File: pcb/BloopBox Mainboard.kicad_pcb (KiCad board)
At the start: 4 copper layers, 65 x 44 mm, 61 parts, among them J1 ExtLED, J2 SPKR, J3 Raspberry_Pi, J4 I2C, J5 NFC-Module, J6 GPIO, J7 TailBoard, J8 PROG, Q1 2N7002, Q2 2N7002, Q3 2N7002, Q4 2N7002, Q5 2N7002, Q6 2N7002, U1 MAX98357, U2 CAT24C32

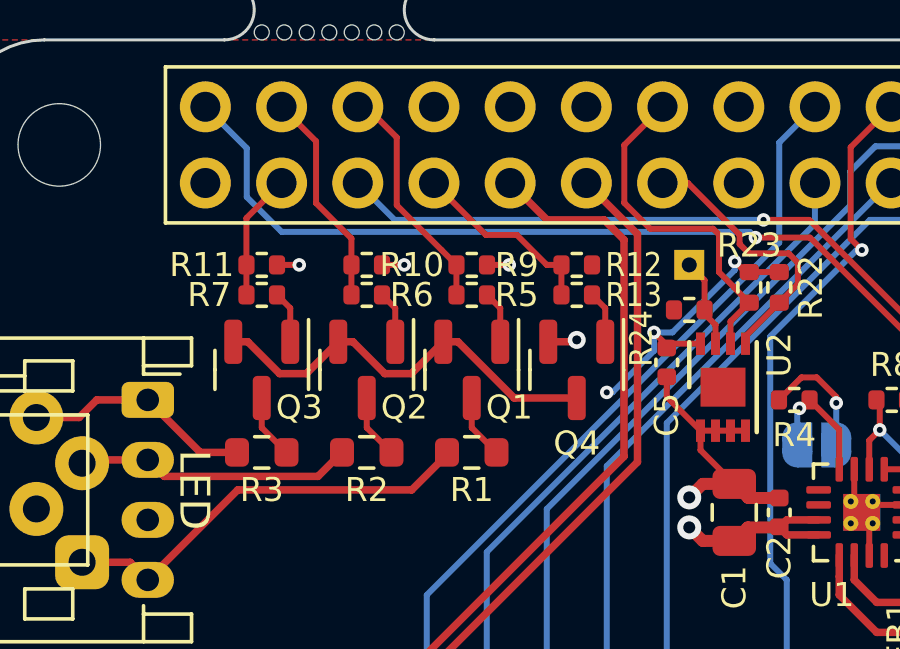
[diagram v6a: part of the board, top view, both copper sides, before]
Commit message: fix: update nets
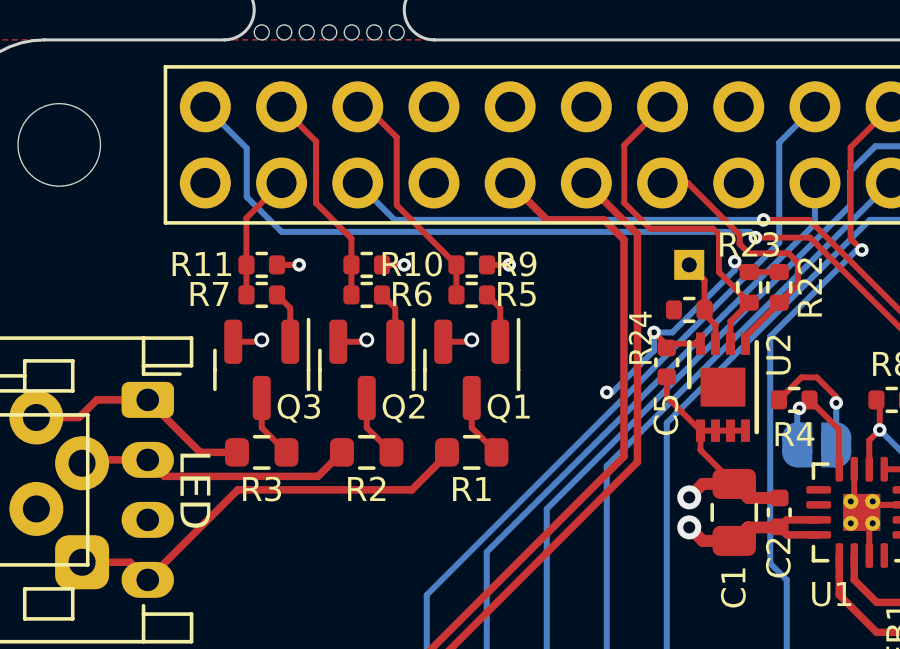
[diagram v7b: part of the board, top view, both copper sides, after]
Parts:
- removed Q4: 2N7002, Package_TO_SOT_SMD:SOT-23
- removed R12: 10k, Resistor_SMD:R_0402_1005Metric
- removed R13: 100R, Resistor_SMD:R_0402_1005Metric
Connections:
- J3 pad 33: /LED_PWM -> unconnected-(J3-Pad33)
- Q1 pad 2: /Pd -> GND
- Q2 pad 2: /Pd -> GND
- Q3 pad 2: /Pd -> GND
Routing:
- net /Pd: track 14.0 -> 0.00 mm
- net /LED_PWM: track 6.38 -> 0.00 mm
- net GND: track 17.0 -> 18.9 mm, vias 7 -> 9
- net /Pg: track 1.74 -> 0.00 mm

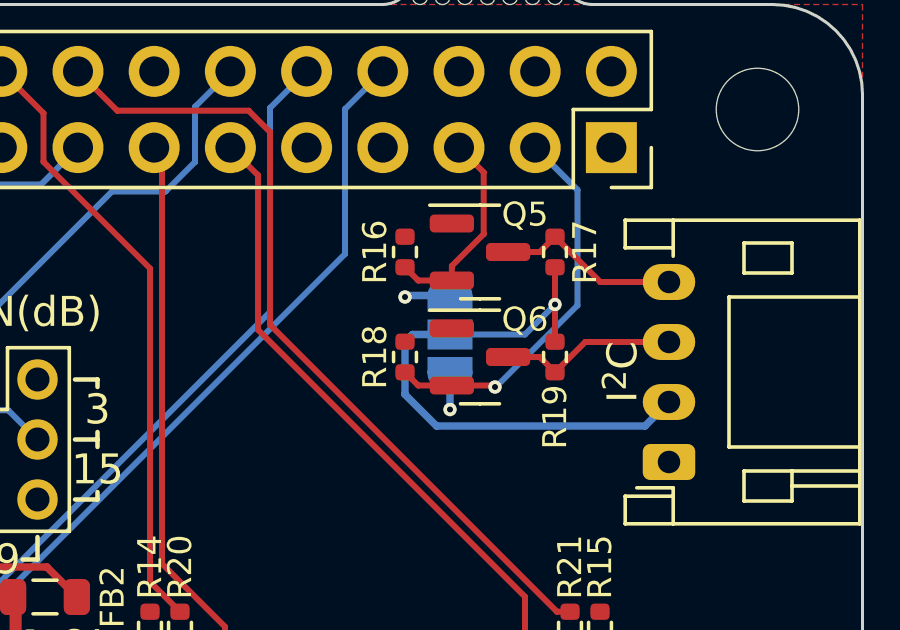
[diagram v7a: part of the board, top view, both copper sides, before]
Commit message: fix: add default connection for I2C voltage jumper
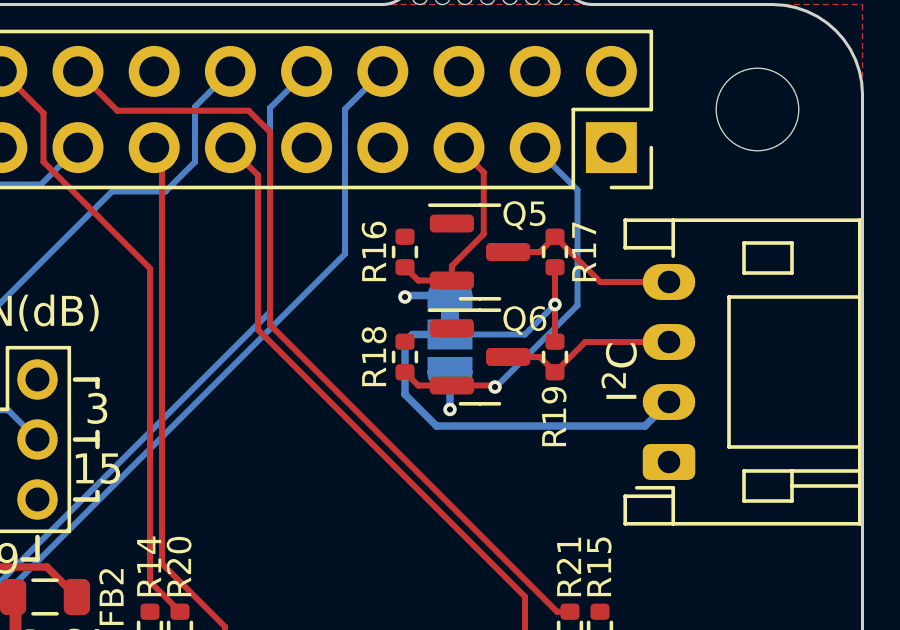
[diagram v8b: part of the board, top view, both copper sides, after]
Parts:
- JP3: value I2C Voltage-Select -> SolderJumper_3_Bridged12; footprint Jumper:SolderJumper-3_P1.3mm_Open_RoundedPad1.0x1.5mm -> Jumper:SolderJumper-3_P1.3mm_Bridged12_RoundedPad1.0x1.5mm
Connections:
- JP3 pad 1: +3V3 -> +5V
- JP3 pad 3: +5V -> +3V3
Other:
- board text added: "5V 3V3"
- board text removed: "3V3 5V"
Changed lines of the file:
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@@
     )
   )
-  (footprint "Jumper:SolderJumper-3_P1.3mm_Open_RoundedPad1.0x1.5mm" (layer "B.Cu")
+  (footprint "Jumper:SolderJumper-3_P1.3mm_Bridged12_RoundedPad1.0x1.5mm" (layer "B.Cu")
     (at 168.75 57.5 -90)
-    (descr "SMD Solder 3-pad Jumper, 1x1.5mm rounded Pads, 0.3mm gap, open")
-    (tags "solder jumper open")
+    (descr "SMD Solder 3-pad Jumper, 1x1.5mm rounded Pads, 0.3mm gap, pads 1-2 bridged with 1 copper strip")
+    (tags "net tie solder jumper bridged")
     (property "Sheetfile" "BloopBox Mainboard.kicad_sch")
     (property "Sheetname" "")
     (attr exclude_from_pos_files)
     (fp_text reference "JP3" (at 0 1.8 90) (layer "B.SilkS") hide
-      (effects (font (size 0.8 0.8) (thickness 0.15)) (justify mirror))
-    )
-    (fp_text value "I2C Voltage-Select" (at 0 -1.9 90) (layer "B.Fab")
       (effects (font (size 1 1) (thickness 0.15)) (justify mirror))
     )
+    (fp_text value "SolderJumper_3_Bridged12" (at 0 -1.9 90) (layer "B.Fab")
+      (effects (font (size 1 1) (thickness 0.15)) (justify mirror))
+    )
+    (fp_poly (pts
+        (xy -0.9 0.3)
+        (xy -0.4 0.3)
+        (xy -0.4 -0.3)
+        (xy -0.9 -0.3)
+      ) (layer "B.Cu") (width 0) (fill solid))
+    (fp_line (start 2.05 0.3) (end 2.05 -0.3) (layer "B.SilkS") (width 0.12))
+    (fp_line (start -1.2 -1.2) (end -1.5 -1.5) (layer "B.SilkS") (width 0.12))
+    (fp_line (start -2.05 -0.3) (end -2.05 0.3) (layer "B.SilkS") (width 0.12))
+    (fp_line (start -1.5 -1.5) (end -0.9 -1.5) (layer "B.SilkS") (width 0.12))
+    (fp_line (start -1.4 1) (end 1.4 1) (layer "B.SilkS") (width 0.12))
+    (fp_line (start -1.2 -1.2) (end -0.9 -1.5) (layer "B.SilkS") (width 0.12))
     (fp_line (start 1.4 -1) (end -1.4 -1) (layer "B.SilkS") (width 0.12))
-    (fp_line (start -1.4 1) (end 1.4 1) (layer "B.SilkS") (width 0.12))
-    (fp_line (start -2.05 -0.3) (end -2.05 0.3) (layer "B.SilkS") (width 0.12))
-    (fp_line (start 2.05 0.3) (end 2.05 -0.3) (layer "B.SilkS") (width 0.12))
+    (fp_arc (start 2.05 0.3) (mid 1.844975 0.794975) (end 1.35 1) (layer "B.SilkS") (width 0.12))
+    (fp_arc (start -2.05 -0.3) (mid -1.844975 -0.794975) (end -1.35 -1) (layer "B.SilkS") (width 0.12))
     (fp_arc (start -1.35 1) (mid -1.844975 0.794975) (end -2.05 0.3) (layer "B.SilkS") (width 0.12))
-    (fp_arc (start -2.05 -0.3) (mid -1.844975 -0.794975) (end -1.35 -1) (layer "B.SilkS") (width 0.12))
-    (fp_arc (start 2.05 0.3) (mid 1.844975 0.794975) (end 1.35 1) (layer "B.SilkS") (width 0.12))
     (fp_arc (start 1.35 -1) (mid 1.844975 -0.794975) (end 2.05 -0.3) (layer "B.SilkS") (width 0.12))
+    (fp_line (start -2.3 1.25) (end -2.3 -1.25) (layer "B.CrtYd") (width 0.05))
+    (fp_line (start 2.3 -1.25) (end 2.3 1.25) (layer "B.CrtYd") (width 0.05))
     (fp_line (start -2.3 1.25) (end 2.3 1.25) (layer "B.CrtYd") (width 0.05))
     (fp_line (start 2.3 -1.25) (end -2.3 -1.25) (layer "B.CrtYd") (width 0.05))
-    (fp_line (start 2.3 -1.25) (end 2.3 1.25) (layer "B.CrtYd") (width 0.05))
-    (fp_line (start -2.3 1.25) (end -2.3 -1.25) (layer "B.CrtYd") (width 0.05))
     (pad "1" smd custom (at -1.3 0 270) (size 1 0.5) (layers "B.Cu" "B.Mask")
-      (net 4 "+3V3") (pinfunction "A") (pintype "passive") (zone_connect 2)
+      (net 3 "+5V") (pinfunction "A") (pintype "passive") (zone_connect 2)
       (options (clearance outline) (anchor rect))
       (primitives
@@
       (net 25 "/V_I2C") (pinfunction "C") (pintype "passive"))
     (pad "3" smd custom (at 1.3 0 270) (size 1 0.5) (layers "B.Cu" "B.Mask")
-      (net 3 "+5V") (pinfunction "B") (pintype "passive") (zone_connect 2)
+      (net 4 "+3V3") (pinfunction "B") (pintype "passive") (zone_connect 2)
       (options (clearance outline) (anchor rect))
       (primitives
@@
     (effects (font (size 1 1) (thickness 0.15)) (justify right mirror))
   )
-  (gr_text "3V3\n5V\n" (at 167.75 57.5) (layer "B.SilkS")
+  (gr_text "5V\n3V3\n" (at 167.75 57.5) (layer "B.SilkS")
     (effects (font (size 1 1) (thickness 0.15)) (justify left mirror))
   )
@@
   (segment (start 146.9 58.4) (end 146.9 58.6) (width 0.2) (layer "F.Cu") (net 3))
   (segment (start 143.5 63.2) (end 143.95 62.75) (width 0.4) (layer "F.Cu") (net 3))
-  (via (at 168.75 60) (size 0.45) (drill 0.2) (layers "F.Cu" "B.Cu") (net 3))
+  (via (at 167.25 56.25) (size 0.45) (drill 0.2) (layers "F.Cu" "B.Cu") (net 3))
   (via (at 142 62.75) (size 0.8) (drill 0.4) (layers "F.Cu" "B.Cu") (net 3))
   (via (at 146.9 58.6) (size 0.45) (drill 0.2) (layers "F.Cu" "B.Cu") (net 3))
-  (segment (start 168.75 58.8) (end 168.75 60) (width 0.25) (layer "B.Cu") (net 3))
+  (segment (start 168.75 56.2) (end 167.3 56.2) (width 0.25) (layer "B.Cu") (net 3))
   (segment (start 146.9 60) (end 146.9 58.6) (width 0.2) (layer "B.Cu") (net 3))
+  (segment (start 167.3 56.2) (end 167.25 56.25) (width 0.25) (layer "B.Cu") (net 3))
   (segment (start 141.25 56.77) (end 141.25 56.6755) (width 0.2) (layer "F.Cu") (net 4))
   (segment (start 143.869839 54.24) (end 145 54.24) (width 0.2) (layer "F.Cu") (net 4))
@@
   (segment (start 142.375 56.625) (end 141.395 56.625) (width 0.2) (layer "F.Cu") (net 4))
   (segment (start 143.517816 53.887977) (end 143.869839 54.24) (width 0.2) (layer "F.Cu") (net 4))
+  (via (at 168.75 60) (size 0.45) (drill 0.2) (layers "F.Cu" "B.Cu") (net 4))
   (via (at 143.517816 53.887977) (size 0.45) (drill 0.2) (layers "F.Cu" "B.Cu") (net 4))
   (via (at 140.8245 56.25) (size 0.45) (drill 0.2) (layers "F.Cu" "B.Cu") (net 4))
-  (via (at 167.25 56.25) (size 0.45) (drill 0.2) (layers "F.Cu" "B.Cu") (net 4))
   (via (at 139.25 58.25) (size 0.45) (drill 0.2) (layers "F.Cu" "B.Cu") (net 4))
   (segment (start 139.439338 58.25) (end 139.25 58.25) (width 0.2) (layer "B.Cu") (net 4))
+  (segment (start 168.75 58.8) (end 168.75 60) (width 0.25) (layer "B.Cu") (net 4))
   (segment (start 143.517816 53.887977) (end 143.517816 54.171522) (width 0.2) (layer "B.Cu") (net 4))
   (segment (start 140.8245 56.864838) (end 139.439338 58.25) (width 0.2) (layer "B.Cu") (net 4))
   (segment (start 140.8245 56.25) (end 140.8245 56.864838) (width 0.2) (layer "B.Cu") (net 4))
   (segment (start 143.517816 54.171522) (end 141.439338 56.25) (width 0.2) (layer "B.Cu") (net 4))
-  (segment (start 168.75 56.2) (end 167.3 56.2) (width 0.25) (layer "B.Cu") (net 4))
   (segment (start 141.439338 56.25) (end 140.8245 56.25) (width 0.2) (layer "B.Cu") (net 4))
-  (segment (start 167.3 56.2) (end 167.25 56.25) (width 0.25) (layer "B.Cu") (net 4))
   (segment (start 125.17 74.25) (end 123.71 72.79) (width 0.2) (layer "B.Cu") (net 6))
   (segment (start 145.815686 74.25) (end 125.17 74.25) (width 0.2) (layer "B.Cu") (net 6))
